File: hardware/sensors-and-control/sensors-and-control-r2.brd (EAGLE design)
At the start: 88 x 79 mm, 79 parts, among them IC1 STM32L496ZET6

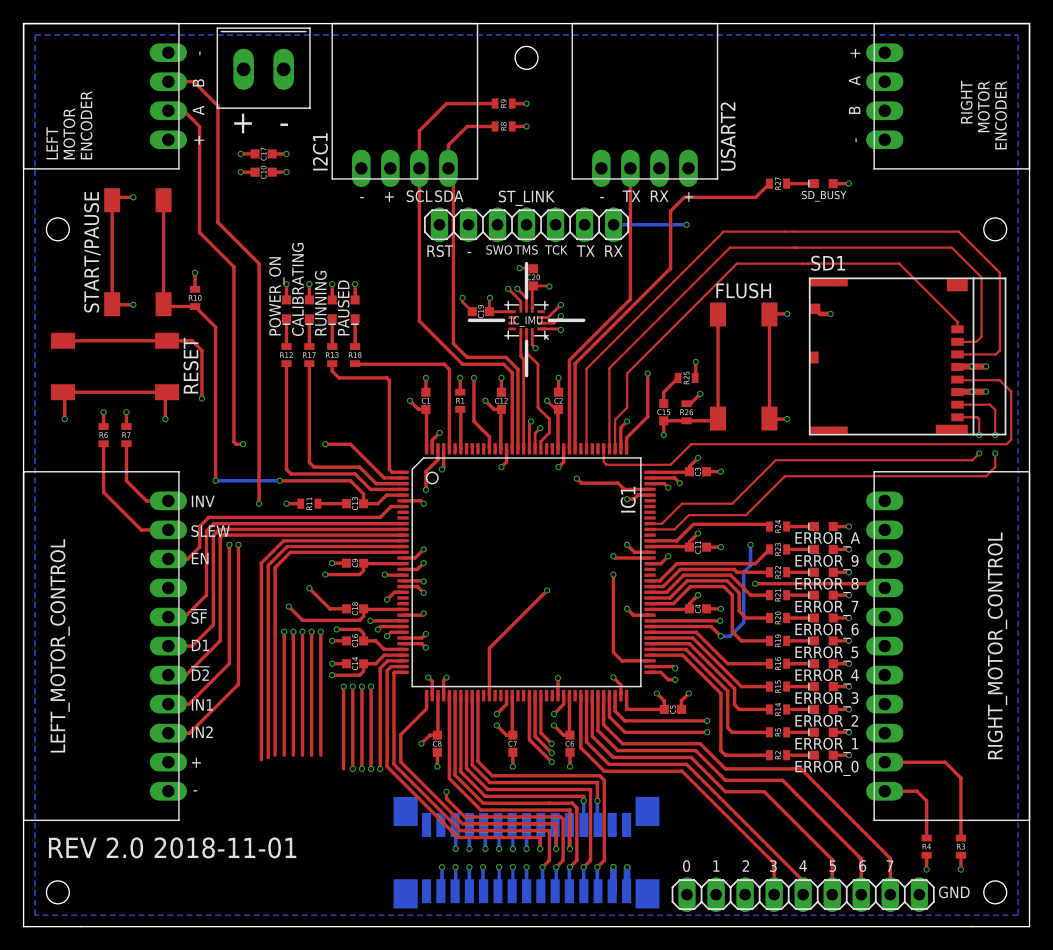
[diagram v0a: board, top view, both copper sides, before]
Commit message: - added a bit of SPI initialization code - moved SD flush to A12 with it's own EXTI - added 2nd revision board (see revision-history.txt for details)
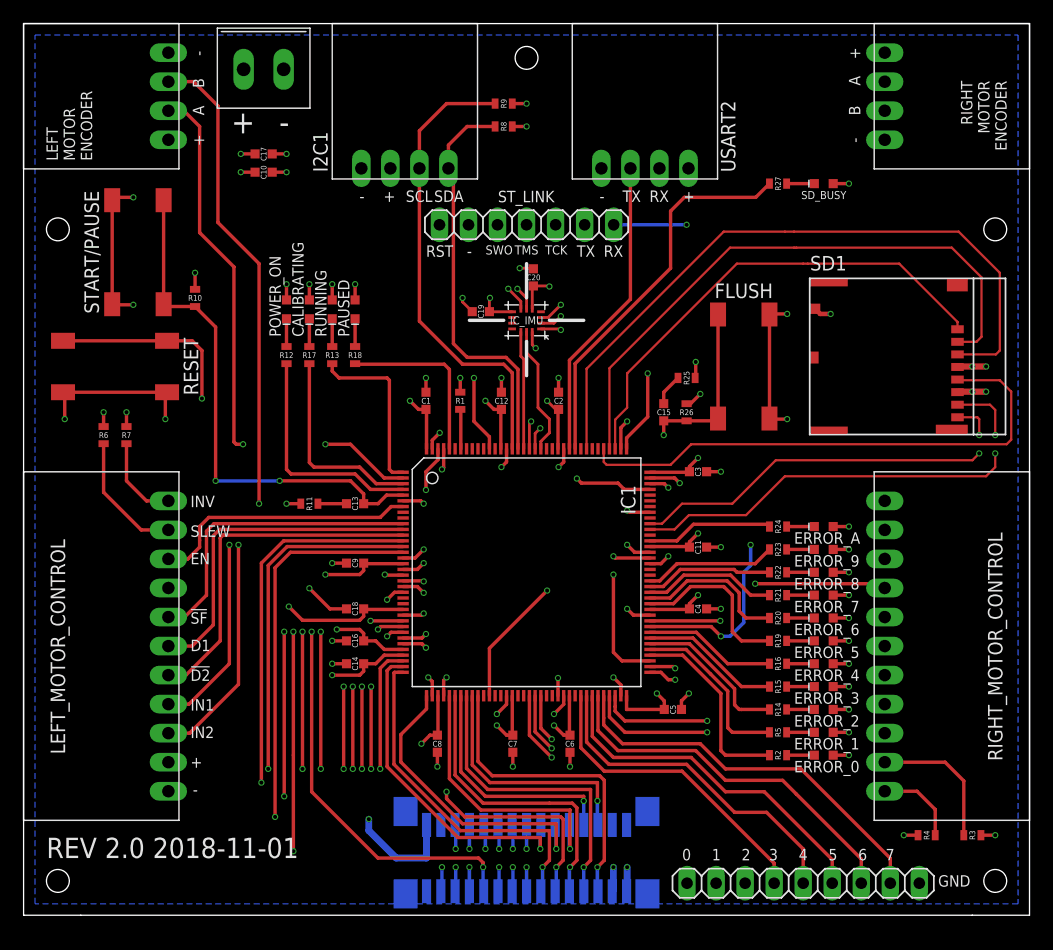
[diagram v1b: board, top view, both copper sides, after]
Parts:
- moved R3 1.41 mm to (83.0, 29.0), turned to 180 degrees
- moved R4 1.00 mm to (79.0, 29.0), turned to 0 degrees
- moved TIMING_OUT 1.00 mm to (68.2, 24.8)
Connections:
- removed net N$46: IC1.101
- new net N$35: IC1.104
- net SD_FLUSH: now also IC1.101; no longer IC1.104
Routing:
- net SENSOR_19: track 24.6 -> 51.0 mm, vias 3 -> 4
- net SENSOR_21: track 30.3 -> 54.6 mm, vias 1 -> 2
- net SENSOR_20: track 29.6 -> 52.3 mm, vias 3 -> 4
- net SENSOR_23: track 32.5 -> 53.8 mm, vias 1 -> 2
- net SENSOR_17: track 26.2 -> 47.3 mm
- net SENSOR_18: track 27.2 -> 47.7 mm, vias 3 -> 4
- net SENSOR_16: track 21.6 -> 42.0 mm, vias 3 -> 4
- net SENSOR_22: track 31.4 -> 51.7 mm, vias 1 -> 2
- net SENSOR_15: track 23.4 -> 43.3 mm, vias 3 -> 4
- net VDD: track 98.8 -> 108.8 mm, vias 27 -> 28
- net TIMING_OUT_2: track 33.7 -> 31.1 mm
- net TIMING_OUT_1: track 32.2 -> 29.8 mm
- net TIMING_OUT_0: track 29.9 -> 28.0 mm
- net TIMING_OUT_3: track 28.7 -> 27.4 mm
- net TIMING_OUT_6: track 34.1 -> 32.9 mm
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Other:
- board size 88 x 79 mm -> 88 x 78 mm

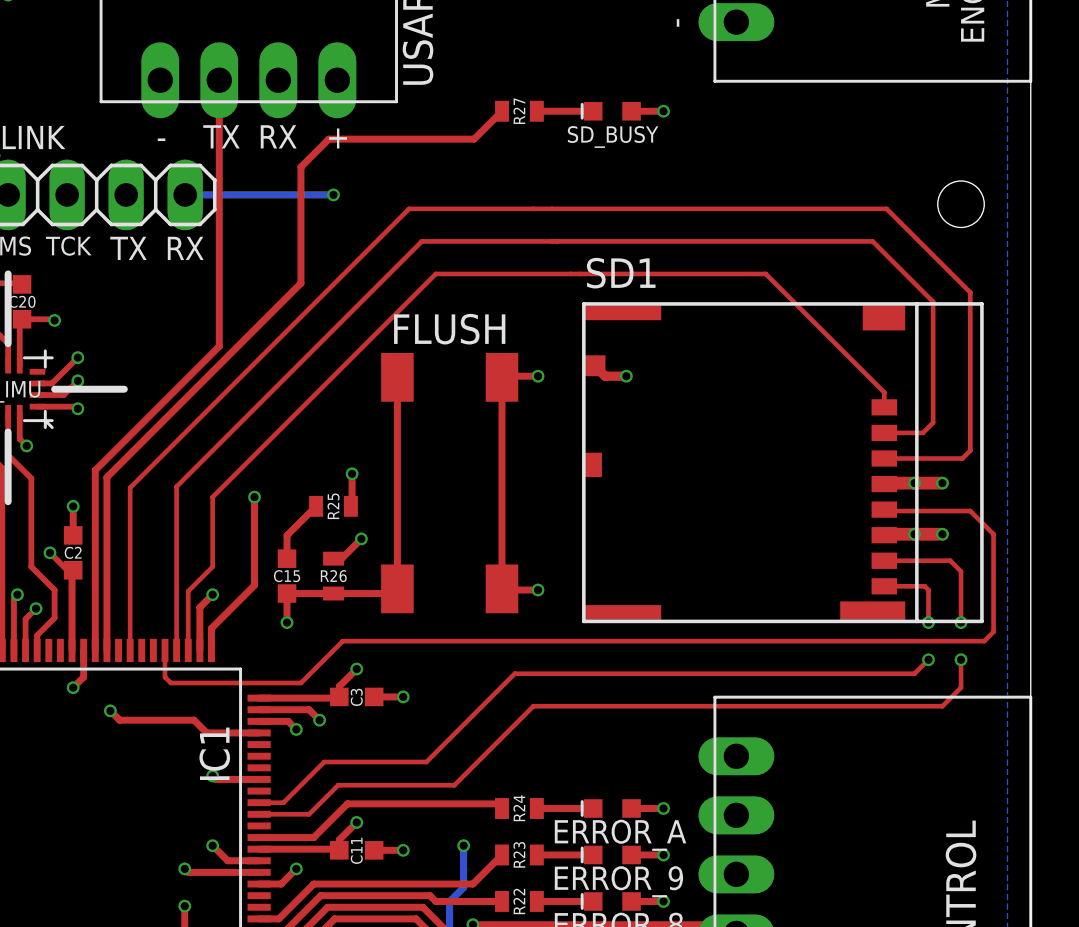
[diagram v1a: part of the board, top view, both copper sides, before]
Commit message: - added SD card detection PIN (D1) - added pullup resistors for SD's D0-D3 and CMD lines (47k)
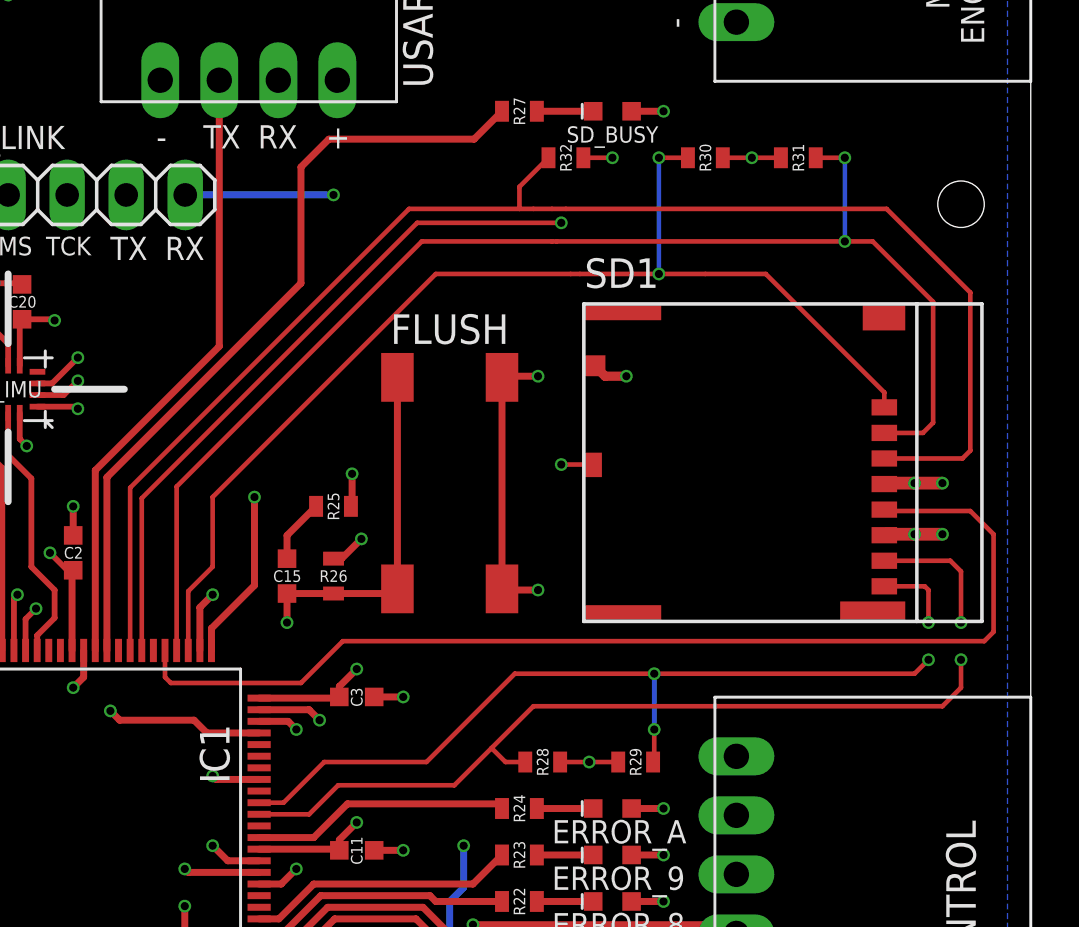
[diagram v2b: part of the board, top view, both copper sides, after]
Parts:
- added R28, R29, R30, R31, R32: 47k, resistors:RESISTOR-0603
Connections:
- removed net N$28: IC1.115
- new net SD_DETECT: IC1.115, SD1.DSM
- net SDMMC1_CMD: now also R32.P$1
- net SDMMC1_D0: now also R28.P$1
- net SDMMC1_D1: now also R29.P$1
- net SDMMC1_D2: now also R30.P$1
- net SDMMC1_D3: now also R31.P$1
- net VDD: now also R28.P$2, R29.P$2, R30.P$2, R31.P$2, R32.P$2
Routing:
- net SD_DETECT: track 0.00 -> 41.3 mm, vias 0 -> 2
- net VDD: track 108.8 -> 115.0 mm, vias 28 -> 31
- net SDMMC1_D2: track 42.7 -> 48.9 mm, vias 0 -> 2
- net SDMMC1_D3: track 52.5 -> 57.4 mm, vias 0 -> 2
- net SDMMC1_D1: track 36.3 -> 40.1 mm, vias 2 -> 4
- net SDMMC1_CMD: track 60.3 -> 63.0 mm
- net SDMMC1_D0: track 40.9 -> 42.6 mm
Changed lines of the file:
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@@
 </element>
 <element name="R27" library="resistors" library_urn="urn:adsk.eagle:library:704770" package="RESISTOR-0603" package3d_urn="urn:adsk.eagle:package:704947/3" value="15k" x="66" y="86" rot="R180"/>
+<element name="R28" library="resistors" library_urn="urn:adsk.eagle:library:704770" package="RESISTOR-0603" package3d_urn="urn:adsk.eagle:package:704947/3" value="47k" x="67" y="58"/>
+<element name="R29" library="resistors" library_urn="urn:adsk.eagle:library:704770" package="RESISTOR-0603" package3d_urn="urn:adsk.eagle:package:704947/3" value="47k" x="71" y="58" rot="R180"/>
+<element name="R30" library="resistors" library_urn="urn:adsk.eagle:library:704770" package="RESISTOR-0603" package3d_urn="urn:adsk.eagle:package:704947/3" value="47k" x="74" y="84"/>
+<element name="R31" library="resistors" library_urn="urn:adsk.eagle:library:704770" package="RESISTOR-0603" package3d_urn="urn:adsk.eagle:package:704947/3" value="47k" x="78" y="84" rot="R180"/>
+<element name="R32" library="resistors" library_urn="urn:adsk.eagle:library:704770" package="RESISTOR-0603" package3d_urn="urn:adsk.eagle:package:704947/3" value="47k" x="68" y="84"/>
 </elements>
 <signals>
@@
 <wire x1="35.25" y1="27" x2="32.6" y2="27" width="0.6" layer="16"/>
 <wire x1="30.2" y1="29.4" x2="30.2" y2="30.4" width="0.6" layer="16"/>
+<contactref element="R32" pad="P$2"/>
+<contactref element="R28" pad="P$2"/>
+<contactref element="R29" pad="P$2"/>
+<contactref element="R30" pad="P$2"/>
+<contactref element="R31" pad="P$2"/>
+<via x="69" y="58" extent="1-16" drill="0.35"/>
+<wire x1="67.75" y1="58" x2="69" y2="58" width="0.2" layer="1"/>
+<wire x1="70.25" y1="58" x2="69" y2="58" width="0.2" layer="1"/>
+<wire x1="74.75" y1="84" x2="76" y2="84" width="0.2" layer="1"/>
+<via x="76" y="84" extent="1-16" drill="0.35"/>
+<wire x1="77.25" y1="84" x2="76" y2="84" width="0.2" layer="1"/>
+<wire x1="68.75" y1="84" x2="70" y2="84" width="0.2" layer="1"/>
+<via x="70" y="84" extent="1-16" drill="0.35"/>
 </signal>
 <signal name="!RESET">
@@
 </signal>
 <signal name="SDMMC1_D0">
-<contactref element="SD1" pad="7"/>
 <contactref element="IC1" pad="98"/>
-<wire x1="85" y1="66.2" x2="84.54" y2="66.66" width="0.2" layer="1"/>
+<wire x1="84.54" y1="66.66" x2="85" y2="66.2" width="0.2" layer="1"/>
 <wire x1="85" y1="66.2" x2="85" y2="64" width="0.2" layer="1"/>
 <via x="85" y="64" extent="1-16" drill="0.35"/>
@@
 <via x="85" y="62.4" extent="1-16" drill="0.35"/>
 <wire x1="85" y1="64" x2="85" y2="62.4" width="0.2" layer="2"/>
-<wire x1="84.54" y1="66.66" x2="81.7" y2="66.66" width="0.2" layer="1"/>
-<wire x1="63.2" y1="57" x2="66.6" y2="60.4" width="0.2" layer="1"/>
+<wire x1="63.2" y1="57" x2="64.8" y2="58.6" width="0.2" layer="1"/>
+<wire x1="64.8" y1="58.6" x2="66.6" y2="60.4" width="0.2" layer="1"/>
 <wire x1="56.95" y1="55.75" x2="58.2" y2="57" width="0.2" layer="1"/>
 <wire x1="58.2" y1="57" x2="63.2" y2="57" width="0.2" layer="1"/>
 <wire x1="66.6" y1="60.4" x2="84.2" y2="60.4" width="0.2" layer="1"/>
+<contactref element="SD1" pad="7"/>
+<contactref element="R28" pad="P$1"/>
+<wire x1="81.7" y1="66.66" x2="84.54" y2="66.66" width="0.2" layer="1"/>
+<wire x1="66.25" y1="58" x2="65.4" y2="58" width="0.2" layer="1"/>
+<wire x1="65.4" y1="58" x2="64.8" y2="58.6" width="0.2" layer="1"/>
 </signal>
 <signal name="SDMMC1_D1">
@@
 <wire x1="65.8" y1="61.8" x2="62" y2="58" width="0.2" layer="1"/>
 <wire x1="62" y1="58" x2="57.6" y2="58" width="0.2" layer="1"/>
-<wire x1="83" y1="61.8" x2="65.8" y2="61.8" width="0.2" layer="1"/>
+<wire x1="83" y1="61.8" x2="71.8" y2="61.8" width="0.2" layer="1"/>
+<contactref element="R29" pad="P$1"/>
+<wire x1="71.8" y1="61.8" x2="65.8" y2="61.8" width="0.2" layer="1"/>
+<wire x1="71.75" y1="58" x2="71.8" y2="58.05" width="0.2" layer="1"/>
+<wire x1="71.8" y1="58.05" x2="71.8" y2="59.4" width="0.2" layer="1"/>
+<via x="71.8" y="59.4" extent="1-16" drill="0.35"/>
+<wire x1="71.8" y1="59.4" x2="71.8" y2="61.8" width="0.2" layer="16"/>
+<via x="71.8" y="61.8" extent="1-16" drill="0.35"/>
 </signal>
 <signal name="SDMMC1_D2">
@@
 <contactref element="IC1" pad="111"/>
 <wire x1="68.2" y1="79" x2="68.6" y2="79" width="0.2" layer="1"/>
-<wire x1="68.6" y1="79" x2="76.6" y2="79" width="0.2" layer="1"/>
+<wire x1="68.6" y1="79" x2="72" y2="79" width="0.2" layer="1"/>
+<wire x1="72" y1="79" x2="74" y2="79" width="0.2" layer="1"/>
+<wire x1="74" y1="79" x2="76.6" y2="79" width="0.2" layer="1"/>
 <wire x1="81.7" y1="73.9" x2="81.7" y2="73.26" width="0.2" layer="1"/>
 <wire x1="76.6" y1="79" x2="81.7" y2="73.9" width="0.2" layer="1"/>
@@
 <wire x1="52.8" y1="69.4" x2="62.4" y2="79" width="0.2" layer="1"/>
 <wire x1="62.4" y1="79" x2="68.2" y2="79" width="0.2" layer="1"/>
+<contactref element="R30" pad="P$1"/>
+<wire x1="73.25" y1="84" x2="72" y2="84" width="0.2" layer="1"/>
+<via x="72" y="84" extent="1-16" drill="0.35"/>
+<wire x1="72" y1="84" x2="72" y2="79" width="0.2" layer="16"/>
+<via x="72" y="79" extent="1-16" drill="0.35"/>
 </signal>
 <signal name="SDMMC1_D3">
@@
 <contactref element="IC1" pad="112"/>
 <wire x1="67.4" y1="80.4" x2="67.6" y2="80.4" width="0.2" layer="1"/>
-<wire x1="67.6" y1="80.4" x2="81.2" y2="80.4" width="0.2" layer="1"/>
+<wire x1="67.6" y1="80.4" x2="80" y2="80.4" width="0.2" layer="1"/>
+<wire x1="80" y1="80.4" x2="81.2" y2="80.4" width="0.2" layer="1"/>
 <wire x1="81.2" y1="80.4" x2="83.8" y2="77.8" width="0.2" layer="1"/>
 <wire x1="83.8" y1="77.8" x2="83.8" y2="72.6" width="0.2" layer="1"/>
@@
 <wire x1="51.25" y1="69.85" x2="61.8" y2="80.4" width="0.2" layer="1"/>
 <wire x1="61.8" y1="80.4" x2="67.4" y2="80.4" width="0.2" layer="1"/>
+<contactref element="R31" pad="P$1"/>
+<wire x1="78.75" y1="84" x2="80" y2="84" width="0.2" layer="1"/>
+<via x="80" y="84" extent="1-16" drill="0.35"/>
+<wire x1="80" y1="84" x2="80" y2="80.4" width="0.2" layer="16"/>
+<via x="80" y="80.4" extent="1-16" drill="0.35"/>
 </signal>
 <signal name="SDMMC1_CK">
@@
 <wire x1="85.06" y1="71.06" x2="81.7" y2="71.06" width="0.2" layer="1"/>
 <wire x1="66.6" y1="81.8" x2="67.4" y2="81.8" width="0.2" layer="1"/>
-<wire x1="67.4" y1="81.8" x2="81.8" y2="81.8" width="0.2" layer="1"/>
+<wire x1="67.4" y1="81.8" x2="68" y2="81.8" width="0.2" layer="1"/>
+<wire x1="68" y1="81.8" x2="81.8" y2="81.8" width="0.2" layer="1"/>
 <wire x1="81.8" y1="81.8" x2="85.4" y2="78.2" width="0.2" layer="1"/>
 <wire x1="85.4" y1="78.2" x2="85.4" y2="71.4" width="0.2" layer="1"/>
@@
 <wire x1="49.25" y1="62.8" x2="49.25" y2="69.8" width="0.2" layer="1"/>
 <wire x1="49.25" y1="69.8" x2="61.25" y2="81.8" width="0.2" layer="1"/>
-<wire x1="61.25" y1="81.8" x2="66.6" y2="81.8" width="0.2" layer="1"/>
+<wire x1="61.25" y1="81.8" x2="66" y2="81.8" width="0.2" layer="1"/>
+<contactref element="R32" pad="P$1"/>
+<wire x1="66" y1="81.8" x2="66.6" y2="81.8" width="0.2" layer="1"/>
+<wire x1="67.25" y1="84" x2="66" y2="82.75" width="0.2" layer="1"/>
+<wire x1="66" y1="82.75" x2="66" y2="81.8" width="0.2" layer="1"/>
 </signal>
 <signal name="RM_ENC_B">
@@
 <contactref element="IC1" pad="114"/>
 </signal>
-<signal name="N$28">
-<contactref element="IC1" pad="115"/>
-</signal>
 <signal name="N$29">
 <contactref element="IC1" pad="117"/>
@@
 <contactref element="IC1" pad="104"/>
 </signal>
+<signal name="SD_DETECT">
+<contactref element="SD1" pad="DSM"/>
+<contactref element="IC1" pad="115"/>
+<wire x1="49.75" y1="62.8" x2="49.75" y2="69.35" width="0.2" layer="1"/>
+<wire x1="61.6" y1="81.2" x2="67.8" y2="81.2" width="0.2" layer="1"/>
+<via x="67.8" y="81.2" extent="1-16" drill="0.35"/>
+<wire x1="49.75" y1="69.35" x2="61.6" y2="81.2" width="0.2" layer="1"/>
+<wire x1="67.8" y1="81.2" x2="67.8" y2="70.8" width="0.2" layer="2"/>
+<wire x1="69.16" y1="70.785" x2="69.145" y2="70.8" width="0.2" layer="1"/>
+<wire x1="69.145" y1="70.8" x2="67.8" y2="70.8" width="0.2" layer="1"/>
+<via x="67.8" y="70.8" extent="1-16" drill="0.35"/>
+</signal>
 </signals>

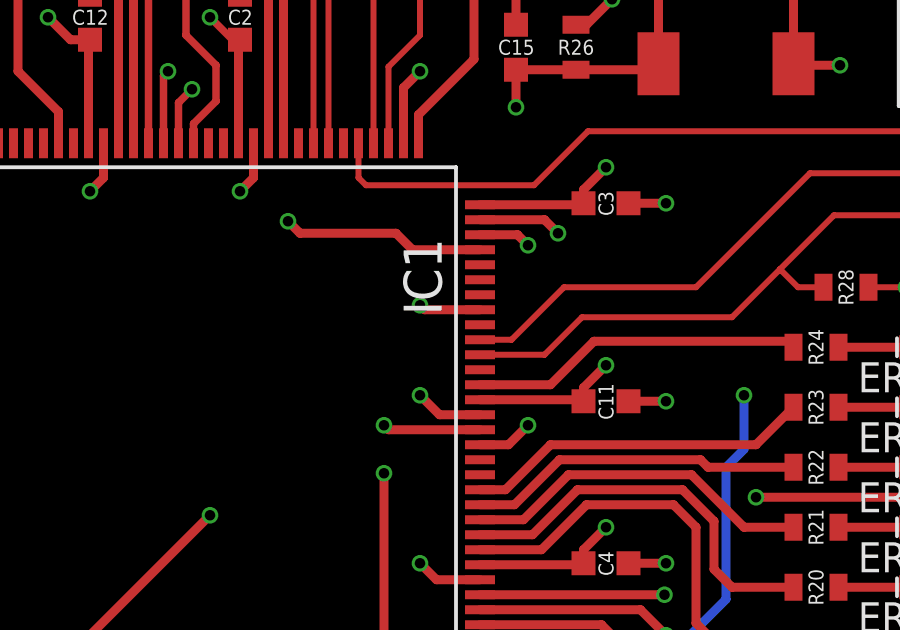
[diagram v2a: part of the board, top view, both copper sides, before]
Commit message: - moved SD_FLUSH to A8
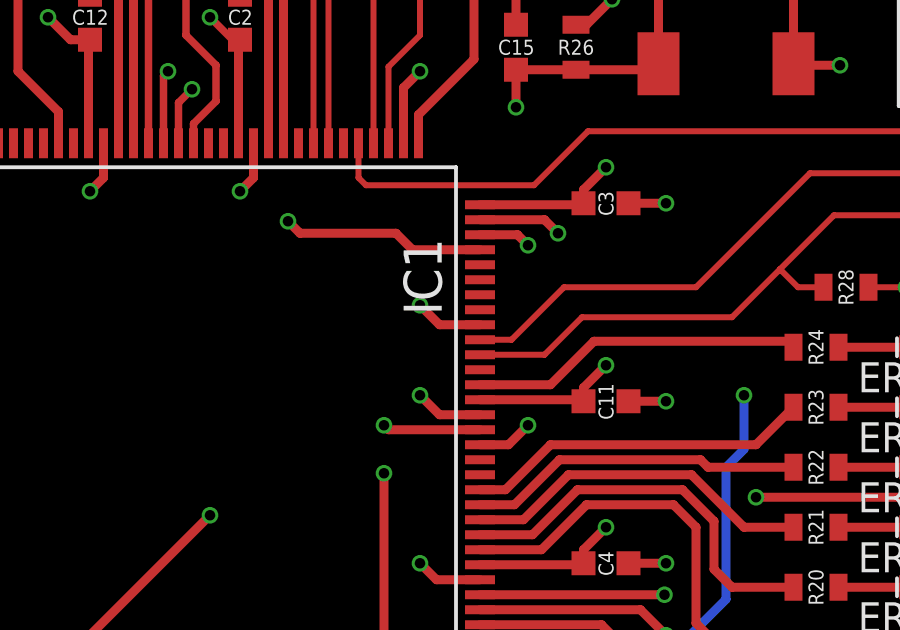
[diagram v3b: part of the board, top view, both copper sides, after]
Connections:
- removed net N$44: IC1.100
- new net N$28: IC1.101
- net SD_FLUSH: now also IC1.100; no longer IC1.101
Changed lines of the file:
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@@
 <contactref element="IC1" pad="9"/>
-</signal>
-<signal name="N$44">
-<contactref element="IC1" pad="100"/>
 </signal>
 <signal name="N$47">
@@
 <wire x1="60.75" y1="74.55" x2="60.75" y2="65.45" width="0.3" layer="1"/>
 <wire x1="60.75" y1="65.45" x2="60.55" y2="65.25" width="0.3" layer="1"/>
-<contactref element="IC1" pad="101"/>
-<wire x1="54.8" y1="57.25" x2="52.95" y2="57.25" width="0.3" layer="1"/>
-<wire x1="52.95" y1="57.25" x2="52.8" y2="57.4" width="0.3" layer="1"/>
 <via x="52.8" y="57.4" extent="1-16" drill="0.35"/>
 <wire x1="52.8" y1="57.4" x2="52.8" y2="60.8" width="0.3" layer="2"/>
+<contactref element="IC1" pad="100"/>
+<wire x1="54.8" y1="56.75" x2="53.45" y2="56.75" width="0.3" layer="1"/>
+<wire x1="53.45" y1="56.75" x2="52.8" y2="57.4" width="0.3" layer="1"/>
 </signal>
 <signal name="N$53">
@@
 <via x="67.8" y="70.8" extent="1-16" drill="0.35"/>
 </signal>
+<signal name="N$28">
+<contactref element="IC1" pad="101"/>
+</signal>
 </signals>
